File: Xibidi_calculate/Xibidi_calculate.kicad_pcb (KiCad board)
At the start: 2 copper layers, 71.1 x 54.2 mm, 62 parts, among them J1 USB_C, SW13 Switch, SW14 Switch, SW15 Switch, SW16 Switch, SW17 Switch, SW18 Switch, SW19 Switch, SW20 Switch, U1 AMS1117-3.3, U11 74LVC2G32, U18 74LVC2G08, U2 74LVC2G86, U20 74LVC2G08, U22 74LVC2G08, U24 74LVC2G08, U4 74LVC2G86, U6 74LVC2G86, U8 74LVC2G86, U9 74LVC2G32

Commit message: fixed silkscreen errors
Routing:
- net Net-(D2-A): vias 5 -> 4
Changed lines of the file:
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@@
 	)
 	(setup
+		(stackup
+			(layer "F.SilkS"
+				(type "Top Silk Screen")
+			)
+			(layer "F.Paste"
+				(type "Top Solder Paste")
+			)
+			(layer "F.Mask"
+				(type "Top Solder Mask")
+				(thickness 0.01)
+			)
+			(layer "F.Cu"
+				(type "copper")
+				(thickness 0.035)
+			)
+			(layer "dielectric 1"
+				(type "core")
+				(thickness 1.51)
+				(material "FR4")
+				(epsilon_r 4.5)
+				(loss_tangent 0.02)
+			)
+			(layer "B.Cu"
+				(type "copper")
+				(thickness 0.035)
+			)
+			(layer "B.Mask"
+				(type "Bottom Solder Mask")
+				(thickness 0.01)
+			)
+			(layer "B.Paste"
+				(type "Bottom Solder Paste")
+			)
+			(layer "B.SilkS"
+				(type "Bottom Silk Screen")
+			)
+			(copper_finish "None")
+			(dielectric_constraints no)
+		)
 		(pad_to_mask_clearance 0)
 		(allow_soldermask_bridges_in_footprints no)
@@
 		(capping no)
 		(filling no)
+		(zone_defaults)
 		(pcbplotparams
 			(layerselection 0x00000000_00000000_55555555_5755f5ff)
@@
 		(tags "switch single-pole opposite-side-connection double-throw SPDT würth wurth")
 		(property "Reference" "SW16"
-			(at 0 -2.54 0)
+			(at 0 -1.945786 0)
 			(layer "F.SilkS")
 			(effects
@@
 		(tags "switch single-pole opposite-side-connection double-throw SPDT würth wurth")
 		(property "Reference" "SW14"
-			(at 0 -2.54 0)
+			(at 0 -1.945786 0)
 			(layer "F.SilkS")
 			(effects
@@
 		(tags "capacitor")
 		(property "Reference" "C7"
-			(at 0 -1.68 90)
+			(at 3.124214 0.044214 90)
 			(layer "F.SilkS")
 			(effects
@@
 			(at 0 -18.25 0)
 			(layer "F.SilkS")
+			(hide yes)
 			(effects
 				(font
@@
 		(sheetname "/")
 		(sheetfile "Xibidi_calculate.kicad_sch")
-		(units
-			(unit
-				(name "A")
-				(pins "SH" "A12" "B12" "A9" "B9" "A5" "B5")
-			)
-		)
 		(attr smd)
 		(duplicate_pad_numbers_are_jumpers no)
 		(fp_line
-			(start -4.58 -1.9)
-			(end -4.58 0.1)
-			(stroke
-				(width 0.12)
-				(type solid)
-			)
-			(layer "F.SilkS")
-		)
-		(fp_line
 			(start -4.58 2)
 			(end -4.58 3.51)
@@
 		)
 		(fp_line
-			(start 4.58 -1.9)
-			(end 4.58 0.1)
-			(stroke
-				(width 0.12)
-				(type solid)
-			)
-			(layer "F.SilkS")
-		)
-		(fp_line
 			(start 4.58 2)
 			(end 4.58 3.51)
@@
 		(tags "switch single-pole opposite-side-connection double-throw SPDT würth wurth")
 		(property "Reference" "SW13"
-			(at 0 -2.54 0)
+			(at 0 -1.945786 0)
 			(layer "F.SilkS")
 			(effects
@@
 		(tags "switch single-pole opposite-side-connection double-throw SPDT würth wurth")
 		(property "Reference" "SW15"
-			(at 0 -2.54 0)
+			(at 0 -1.945786 0)
 			(layer "F.SilkS")
 			(effects
@@
 	)
 	(segment
-		(start 111.959214 131.560786)
-		(end 111.484214 132.035786)
+		(start 95.234214 127.675786)
+		(end 95.464214 127.445786)
 		(width 0.2)
 		(layer "F.Cu")
-		(net "Net-(D4-K)")
+		(net "Net-(D2-K)")
 	)
 	(segment
-		(start 111.734214 127.670786)
-		(end 111.959214 127.445786)
+		(start 95.464214 127.445786)
+		(end 95.464214 131.615786)
 		(width 0.2)
 		(layer "F.Cu")
-		(net "Net-(D4-K)")
+		(net "Net-(D2-K)")
 	)
 	(segment
-		(start 111.959214 127.445786)
-		(end 111.959214 131.560786)
+		(start 95.464214 131.615786)
+		(end 94.994214 132.085786)
 		(width 0.2)
 		(layer "F.Cu")
-		(net "Net-(D4-K)")
+		(net "Net-(D2-K)")
 	)
 	(segment
@@
 	)
 	(segment
-		(start 120.234214 127.445786)
-		(end 120.234214 131.615786)
+		(start 86.734214 127.905786)
+		(end 87.194214 127.445786)
 		(width 0.2)
 		(layer "F.Cu")
-		(net "Net-(D5-K)")
+		(net "Net-(D1-K)")
 	)
 	(segment
-		(start 120.234214 131.615786)
-		(end 119.804214 132.045786)
+		(start 87.194214 131.605786)
+		(end 86.764214 132.035786)
 		(width 0.2)
 		(layer "F.Cu")
-		(net "Net-(D5-K)")
+		(net "Net-(D1-K)")
 	)
 	(segment
-		(start 119.734214 127.945786)
-		(end 120.234214 127.445786)
+		(start 87.194214 127.445786)
+		(end 87.194214 131.605786)
 		(width 0.2)
 		(layer "F.Cu")
-		(net "Net-(D5-K)")
+		(net "Net-(D1-K)")
 	)
 	(segment
@@
 	)
 	(segment
-		(start 95.234214 127.675786)
-		(end 95.464214 127.445786)
-		(width 0.2)
-		(layer "F.Cu")
-		(net "Net-(D2-K)")
-	)
-	(segment
-		(start 95.464214 127.445786)
-		(end 95.464214 131.615786)
-		(width 0.2)
-		(layer "F.Cu")
-		(net "Net-(D2-K)")
-	)
-	(segment
-		(start 95.464214 131.615786)
-		(end 94.994214 132.085786)
-		(width 0.2)
-		(layer "F.Cu")
-		(net "Net-(D2-K)")
-	)
-	(segment
 		(start 106.504214 118.945786)
 		(end 98.004214 127.445786)
@@
 	)
 	(via
-		(at 140.659949 106.733211)
-		(size 0.6)
-		(drill 0.3)
-		(layers "F.Cu" "B.Cu")
-		(net "Net-(D2-A)")
-	)
-	(via
 		(at 137.334214 105.945786)
 		(size 0.6)
@@
 	)
 	(segment
+		(start 111.959214 131.560786)
+		(end 111.484214 132.035786)
+		(width 0.2)
+		(layer "F.Cu")
+		(net "Net-(D4-K)")
+	)
+	(segment
+		(start 111.734214 127.670786)
+		(end 111.959214 127.445786)
+		(width 0.2)
+		(layer "F.Cu")
+		(net "Net-(D4-K)")
+	)
+	(segment
+		(start 111.959214 127.445786)
+		(end 111.959214 131.560786)
+		(width 0.2)
+		(layer "F.Cu")
+		(net "Net-(D4-K)")
+	)
+	(segment
 		(start 128.985685 120.145786)
 		(end 128.88495 120.04505)
@@
 	)
 	(segment
-		(start 86.734214 127.905786)
-		(end 87.194214 127.445786)
-		(width 0.2)
-		(layer "F.Cu")
-		(net "Net-(D1-K)")
-	)
-	(segment
-		(start 87.194214 131.605786)
-		(end 86.764214 132.035786)
-		(width 0.2)
-		(layer "F.Cu")
-		(net "Net-(D1-K)")
-	)
-	(segment
-		(start 87.194214 127.445786)
-		(end 87.194214 131.605786)
-		(width 0.2)
-		(layer "F.Cu")
-		(net "Net-(D1-K)")
-	)
-	(segment
 		(start 138.459214 114.695786)
 		(end 138.384214 114.620786)
@@
 	)
 	(segment
+		(start 120.234214 127.445786)
+		(end 120.234214 131.615786)
+		(width 0.2)
+		(layer "F.Cu")
+		(net "Net-(D5-K)")
+	)
+	(segment
+		(start 120.234214 131.615786)
+		(end 119.804214 132.045786)
+		(width 0.2)
+		(layer "F.Cu")
+		(net "Net-(D5-K)")
+	)
+	(segment
+		(start 119.734214 127.945786)
+		(end 120.234214 127.445786)
+		(width 0.2)
+		(layer "F.Cu")
+		(net "Net-(D5-K)")
+	)
+	(segment

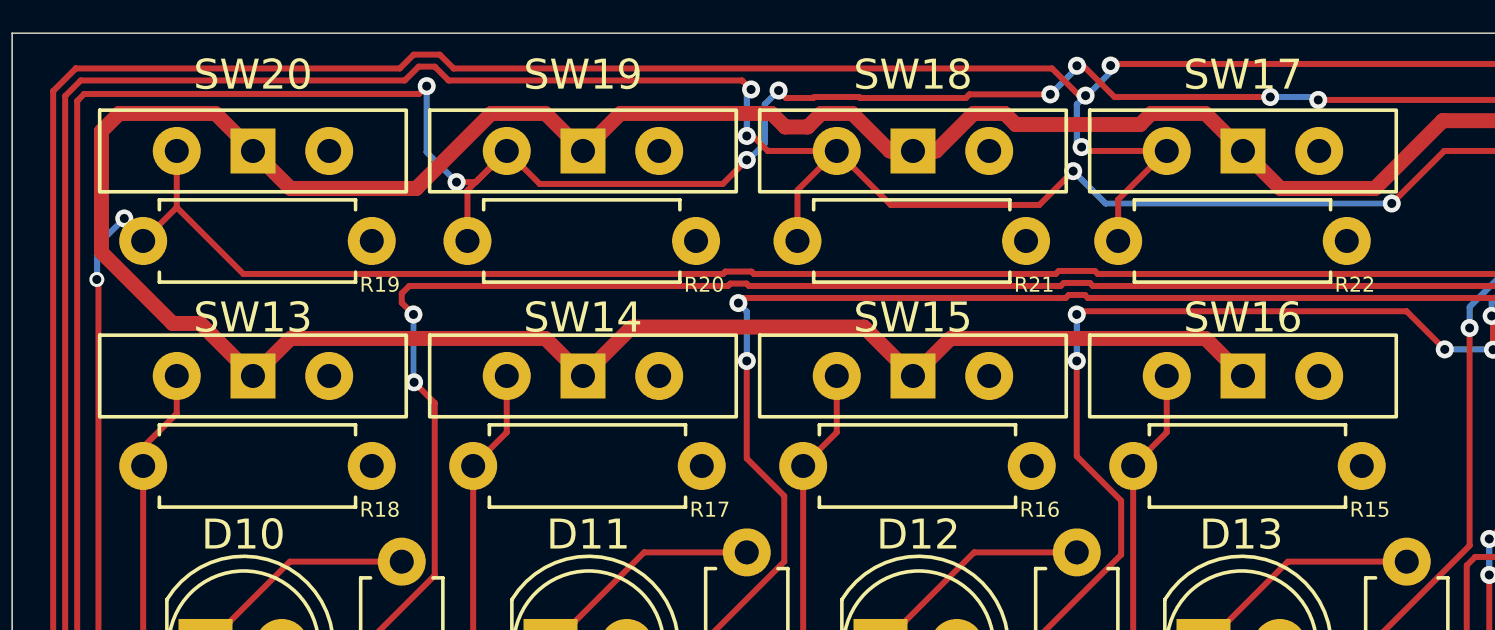
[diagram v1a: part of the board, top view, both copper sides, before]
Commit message: Moved overlapping silkscreen slightly
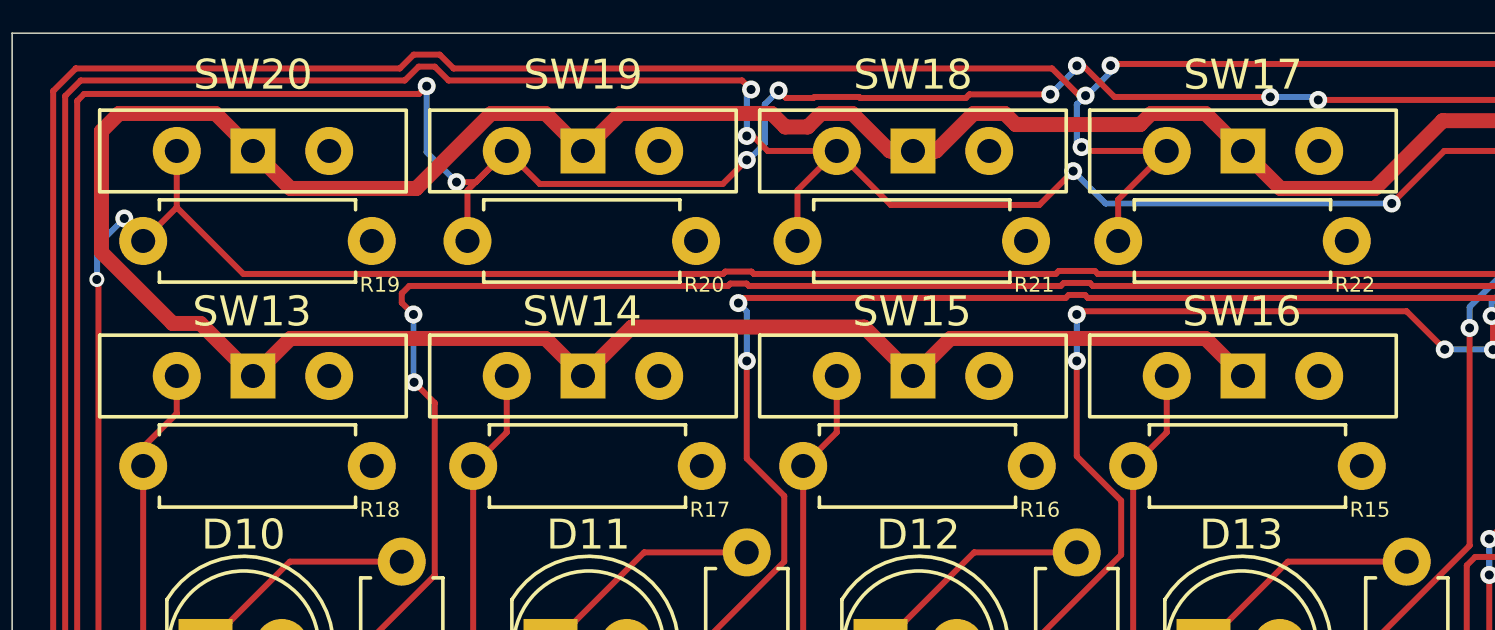
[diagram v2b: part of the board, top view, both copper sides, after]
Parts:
- J1: value USB_C -> USB_C_Receptacle_PowerOnly_6P
